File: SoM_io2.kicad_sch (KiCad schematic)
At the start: 1 part, among them J1 Hermaphroditic_Molex_203456-0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

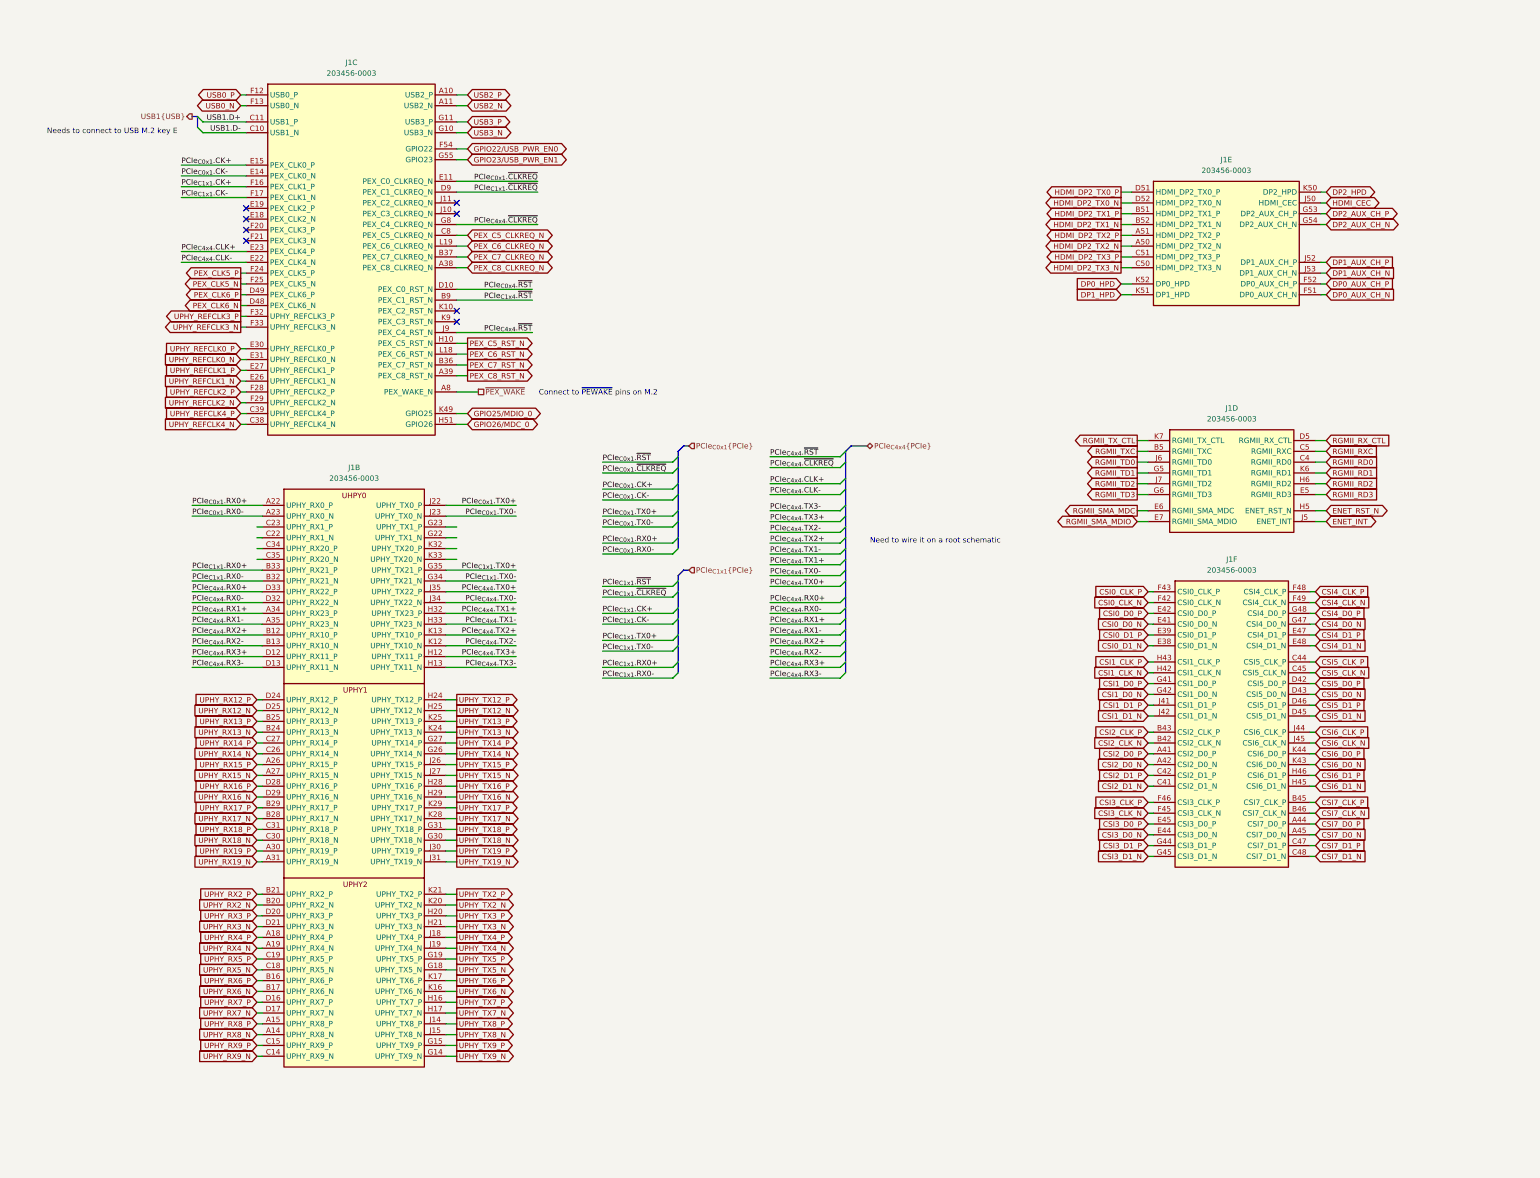
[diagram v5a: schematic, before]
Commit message: [#81970] Connect SFI to SOM
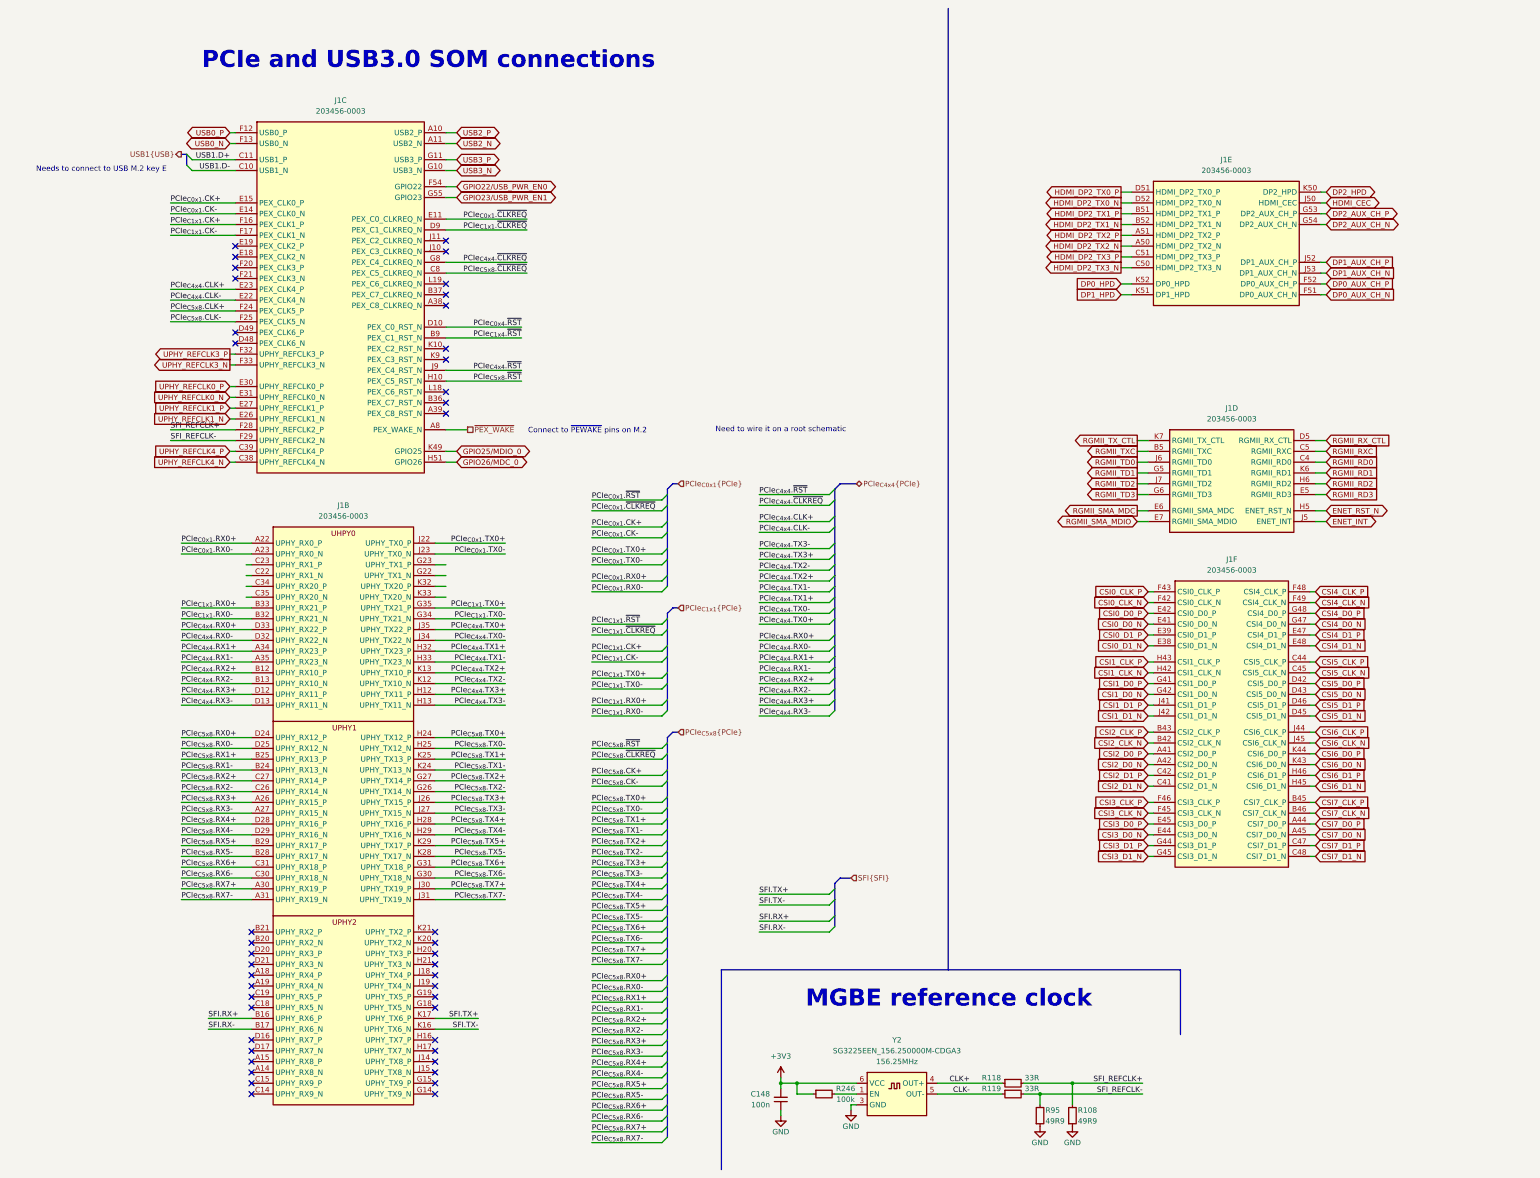
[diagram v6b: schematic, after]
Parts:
- added C148: C_100n_0402, antmicro-footprints:C_0402_1005Metric, symbol antmicroCapacitors0402:C_100n_0402
- added R108, R95: R_49R9_0402, antmicro-footprints:R_0402_1005Metric, symbol antmicroResistors0402:R_49R9_0402
- added R118, R119: R_33R_0402, antmicro-footprints:R_0402_1005Metric, symbol antmicroResistors0402:R_33R_0402
- added R246: R_100k_0402, antmicro-footprints:R_0402_1005Metric, symbol antmicroResistors0402:R_100k_0402
- added Y2: Oscillator_156.25MHz_SG3225EEN, antmicro-footprints:Oscillator_SMD_Epson_SG3225EEN_3.2x2.5x1.2mm, symbol antmicroOscillators:Oscillator_156.25MHz_SG3225EEN
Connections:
- net PEX_C5_CLKREQ_N renamed PCIe_{C5x8}.~{CLKREQ}
- net PEX_C5_RST_N renamed PCIe_{C5x8}.~{RST}
- net PEX_C6_CLKREQ_N: no longer names the net of J1.L19 (PEX_C6_CLKREQ_N)
- net PEX_C6_RST_N: no longer names the net of J1.L18 (PEX_C6_RST_N)
- net PEX_C7_CLKREQ_N: no longer names the net of J1.B37 (PEX_C7_CLKREQ_N)
- net PEX_C7_RST_N: no longer names the net of J1.B36 (PEX_C7_RST_N)
- net PEX_C8_CLKREQ_N: no longer names the net of J1.A38 (PEX_C8_CLKREQ_N)
- net PEX_C8_RST_N: no longer names the net of J1.A39 (PEX_C8_RST_N)
- net PEX_CLK5_N renamed PCIe_{C5x8}.CLK-
- net PEX_CLK5_P renamed PCIe_{C5x8}.CLK+
- net PEX_CLK6_N: no longer names the net of J1.D48 (PEX_CLK6_N)
- net PEX_CLK6_P: no longer names the net of J1.D49 (PEX_CLK6_P)
- net UPHY_REFCLK2_N renamed SFI_REFCLK-
- net SFI_REFCLK-: now also R119.2, R95.2
- net UPHY_REFCLK2_P renamed SFI_REFCLK+
- net SFI_REFCLK+: now also R108.2, R118.2
- net UPHY_RX12_N renamed PCIe_{C5x8}.RX0-
- net UPHY_RX12_P renamed PCIe_{C5x8}.RX0+
- net UPHY_RX13_N renamed PCIe_{C5x8}.RX1-
- net UPHY_RX13_P renamed PCIe_{C5x8}.RX1+
- net UPHY_RX14_N renamed PCIe_{C5x8}.RX2-
- net UPHY_RX14_P renamed PCIe_{C5x8}.RX2+
- net UPHY_RX15_N renamed PCIe_{C5x8}.RX3-
- net UPHY_RX15_P renamed PCIe_{C5x8}.RX3+
- net UPHY_RX16_N renamed PCIe_{C5x8}.RX4-
- net UPHY_RX16_P renamed PCIe_{C5x8}.RX4+
- net UPHY_RX17_N renamed PCIe_{C5x8}.RX5-
- net UPHY_RX17_P renamed PCIe_{C5x8}.RX5+
- net UPHY_RX18_N renamed PCIe_{C5x8}.RX6-
- net UPHY_RX18_P renamed PCIe_{C5x8}.RX6+
- net UPHY_RX19_N renamed PCIe_{C5x8}.RX7-
- net UPHY_RX19_P renamed PCIe_{C5x8}.RX7+
- net UPHY_RX2_N: no longer names the net of J1.B20 (UPHY_RX2_N)
- net UPHY_RX2_P: no longer names the net of J1.B21 (UPHY_RX2_P)
- net UPHY_RX3_N: no longer names the net of J1.D21 (UPHY_RX3_N)
- net UPHY_RX3_P: no longer names the net of J1.D20 (UPHY_RX3_P)
- net UPHY_RX4_N: no longer names the net of J1.A19 (UPHY_RX4_N)
- net UPHY_RX4_P: no longer names the net of J1.A18 (UPHY_RX4_P)
- net UPHY_RX5_N: no longer names the net of J1.C18 (UPHY_RX5_N)
- net UPHY_RX5_P: no longer names the net of J1.C19 (UPHY_RX5_P)
- net UPHY_RX6_N renamed SFI.RX-
- net UPHY_RX6_P renamed SFI.RX+
- net UPHY_RX7_N: no longer names the net of J1.D17 (UPHY_RX7_N)
- net UPHY_RX7_P: no longer names the net of J1.D16 (UPHY_RX7_P)
- net UPHY_RX8_N: no longer names the net of J1.A14 (UPHY_RX8_N)
- net UPHY_RX8_P: no longer names the net of J1.A15 (UPHY_RX8_P)
- net UPHY_RX9_N: no longer names the net of J1.C14 (UPHY_RX9_N)
- net UPHY_RX9_P: no longer names the net of J1.C15 (UPHY_RX9_P)
- net UPHY_TX12_N renamed PCIe_{C5x8}.TX0-
- net UPHY_TX12_P renamed PCIe_{C5x8}.TX0+
- net UPHY_TX13_N renamed PCIe_{C5x8}.TX1-
- net UPHY_TX13_P renamed PCIe_{C5x8}.TX1+
- net UPHY_TX14_N renamed PCIe_{C5x8}.TX2-
- net UPHY_TX14_P renamed PCIe_{C5x8}.TX2+
- net UPHY_TX15_N renamed PCIe_{C5x8}.TX3-
- net UPHY_TX15_P renamed PCIe_{C5x8}.TX3+
- net UPHY_TX16_N renamed PCIe_{C5x8}.TX4-
- net UPHY_TX16_P renamed PCIe_{C5x8}.TX4+
- net UPHY_TX17_N renamed PCIe_{C5x8}.TX5-
- net UPHY_TX17_P renamed PCIe_{C5x8}.TX5+
- net UPHY_TX18_N renamed PCIe_{C5x8}.TX6-
- net UPHY_TX18_P renamed PCIe_{C5x8}.TX6+
- net UPHY_TX19_N renamed PCIe_{C5x8}.TX7-
- net UPHY_TX19_P renamed PCIe_{C5x8}.TX7+
- net UPHY_TX2_N: no longer names the net of J1.K20 (UPHY_TX2_N)
- net UPHY_TX2_P: no longer names the net of J1.K21 (UPHY_TX2_P)
- net UPHY_TX3_N: no longer names the net of J1.H21 (UPHY_TX3_N)
- net UPHY_TX3_P: no longer names the net of J1.H20 (UPHY_TX3_P)
- net UPHY_TX4_N: no longer names the net of J1.J19 (UPHY_TX4_N)
- net UPHY_TX4_P: no longer names the net of J1.J18 (UPHY_TX4_P)
- net UPHY_TX5_N: no longer names the net of J1.G18 (UPHY_TX5_N)
- net UPHY_TX5_P: no longer names the net of J1.G19 (UPHY_TX5_P)
- net UPHY_TX6_N renamed SFI.TX-
- net UPHY_TX6_P renamed SFI.TX+
- net UPHY_TX7_N: no longer names the net of J1.H17 (UPHY_TX7_N)
- net UPHY_TX7_P: no longer names the net of J1.H16 (UPHY_TX7_P)
- net UPHY_TX8_N: no longer names the net of J1.J15 (UPHY_TX8_N)
- net UPHY_TX8_P: no longer names the net of J1.J14 (UPHY_TX8_P)
- net UPHY_TX9_N: no longer names the net of J1.G14 (UPHY_TX9_N)
- net UPHY_TX9_P: no longer names the net of J1.G15 (UPHY_TX9_P)
- new net: R246.2, Y2.1 (EN)
- new net +3V3: C148.2, R246.1, Y2.6 (VCC)
- new net CLK+: R118.1, Y2.4 (OUT+)
- new net CLK-: R119.1, Y2.5 (OUT-)
- new net GND: C148.1, R108.1, R95.1, Y2.3 (GND)
- no-connect marks 8 -> 44
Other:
- note added: "MGBE reference clock"
- note added: "PCIe and USB3.0 SOM connections"
- moved on the sheet: J1B, J1C

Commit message: [#81970] Finalize connecting SFP+ to SOM
[#82054] Update SoM pins definitions

[#82054] Continue work on I2C

[#82330] Clean up

[#81970] Add SFP sheet and power section

[#82330] Annotation and clean up
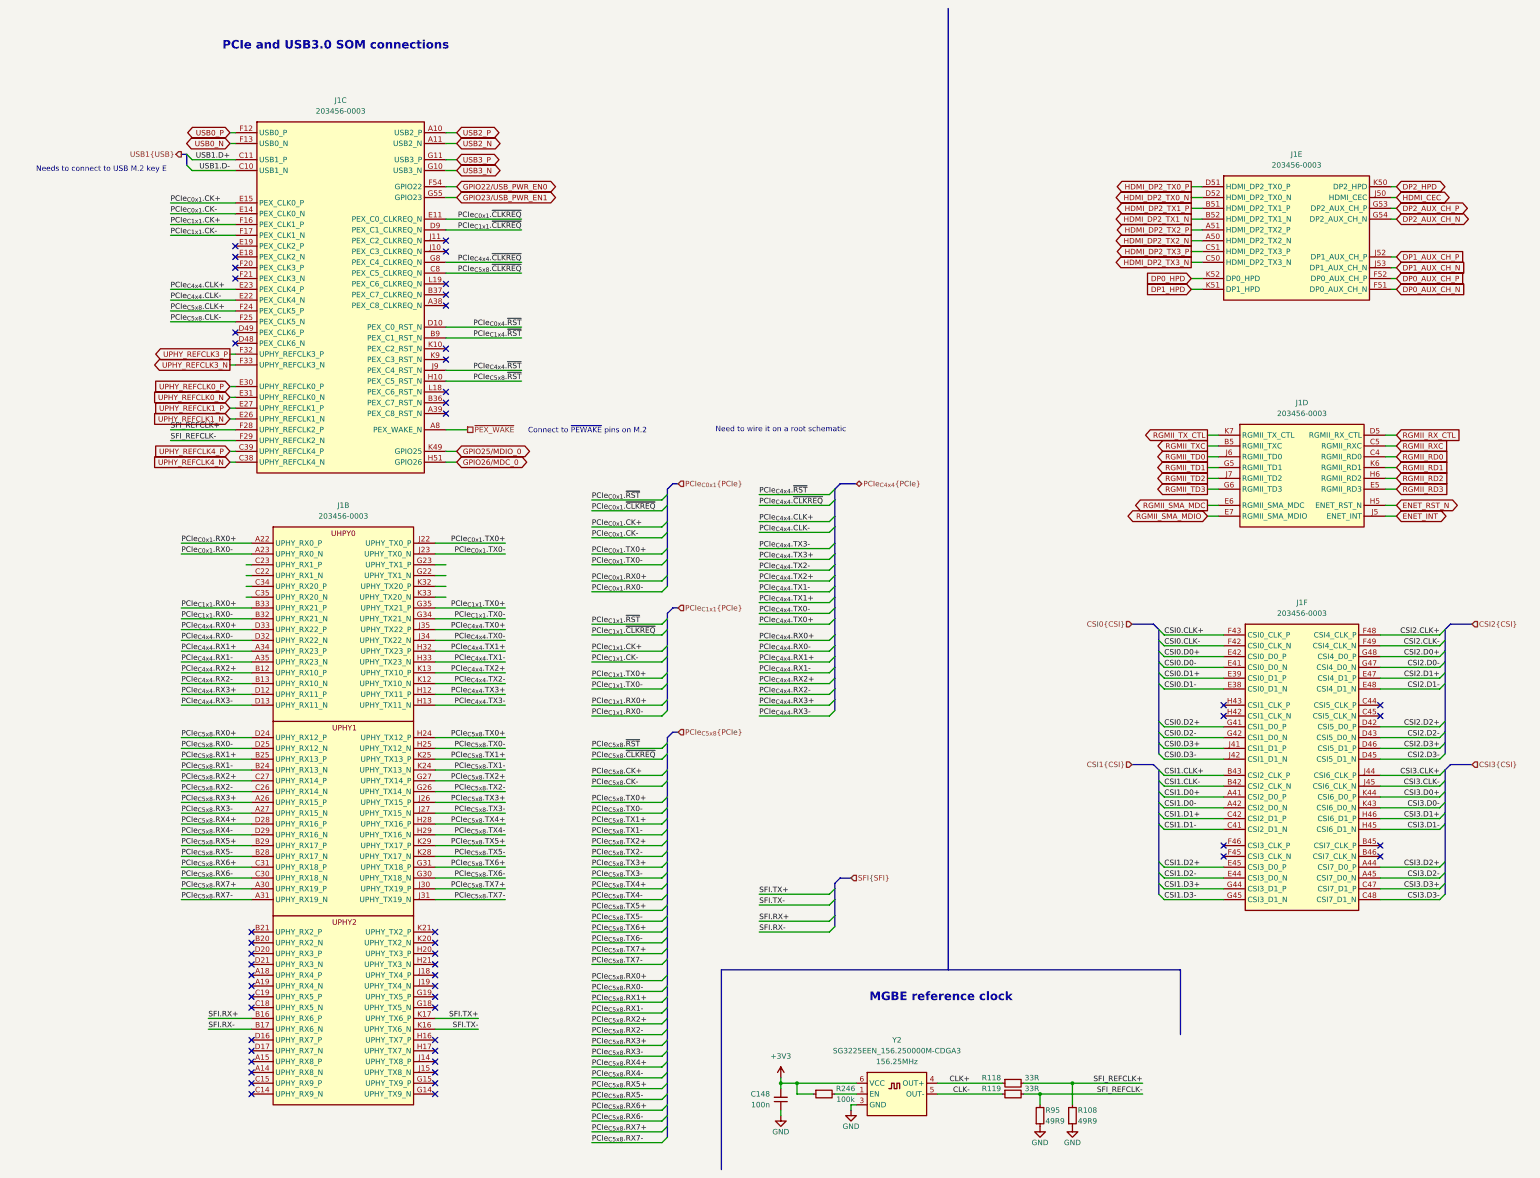
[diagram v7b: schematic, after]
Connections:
- net CSI0_CLK_N renamed CSI0.CLK-
- net CSI0_CLK_P renamed CSI0.CLK+
- net CSI0_D0_N renamed CSI0.D0-
- net CSI0_D0_P renamed CSI0.D0+
- net CSI0_D1_N renamed CSI0.D1-
- net CSI0_D1_P renamed CSI0.D1+
- net CSI1_CLK_N: no longer names the net of J1.H42 (CSI1_CLK_N)
- net CSI1_CLK_P: no longer names the net of J1.H43 (CSI1_CLK_P)
- net CSI1_D0_N renamed CSI0.D2-
- net CSI1_D0_P renamed CSI0.D2+
- net CSI1_D1_N renamed CSI0.D3-
- net CSI1_D1_P renamed CSI0.D3+
- net CSI2_CLK_N renamed CSI1.CLK-
- net CSI2_CLK_P renamed CSI1.CLK+
- net CSI2_D0_N renamed CSI1.D0-
- net CSI2_D0_P renamed CSI1.D0+
- net CSI2_D1_N renamed CSI1.D1-
- net CSI2_D1_P renamed CSI1.D1+
- net CSI3_CLK_N: no longer names the net of J1.F45 (CSI3_CLK_N)
- net CSI3_CLK_P: no longer names the net of J1.F46 (CSI3_CLK_P)
- net CSI3_D0_N renamed CSI1.D2-
- net CSI3_D0_P renamed CSI1.D2+
- net CSI3_D1_N renamed CSI1.D3-
- net CSI3_D1_P renamed CSI1.D3+
- net CSI4_CLK_N renamed CSI2.CLK-
- net CSI4_CLK_P renamed CSI2.CLK+
- net CSI4_D0_N renamed CSI2.D0-
- net CSI4_D0_P renamed CSI2.D0+
- net CSI4_D1_N renamed CSI2.D1-
- net CSI4_D1_P renamed CSI2.D1+
- net CSI5_CLK_N: no longer names the net of J1.C45 (CSI5_CLK_N)
- net CSI5_CLK_P: no longer names the net of J1.C44 (CSI5_CLK_P)
- net CSI5_D0_N renamed CSI2.D2-
- net CSI5_D0_P renamed CSI2.D2+
- net CSI5_D1_N renamed CSI2.D3-
- net CSI5_D1_P renamed CSI2.D3+
- net CSI6_CLK_N renamed CSI3.CLK-
- net CSI6_CLK_P renamed CSI3.CLK+
- net CSI6_D0_N renamed CSI3.D0-
- net CSI6_D0_P renamed CSI3.D0+
- net CSI6_D1_N renamed CSI3.D1-
- net CSI6_D1_P renamed CSI3.D1+
- net CSI7_CLK_N: no longer names the net of J1.B46 (CSI7_CLK_N)
- net CSI7_CLK_P: no longer names the net of J1.B45 (CSI7_CLK_P)
- net CSI7_D0_N renamed CSI3.D2-
- net CSI7_D0_P renamed CSI3.D2+
- net CSI7_D1_N renamed CSI3.D3-
- net CSI7_D1_P renamed CSI3.D3+
- no-connect marks 44 -> 52
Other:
- moved on the sheet: J1D, J1E, J1F
